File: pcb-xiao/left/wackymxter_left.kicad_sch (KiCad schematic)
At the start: 81 parts, among them U1 xiao-ble, U2 74HC595

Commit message: Insane progresgress
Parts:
- U1: footprint mcu:xiao-ble-smd-cutout -> wackymxter:xiao-ble-smd-cutout
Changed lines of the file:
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@@
 			)
 		)
-		(property "Footprint" "mcu:xiao-ble-smd-cutout"
+		(property "Footprint" "wackymxter:xiao-ble-smd-cutout"
 			(at 39.37 43.18 0)
 			(effects

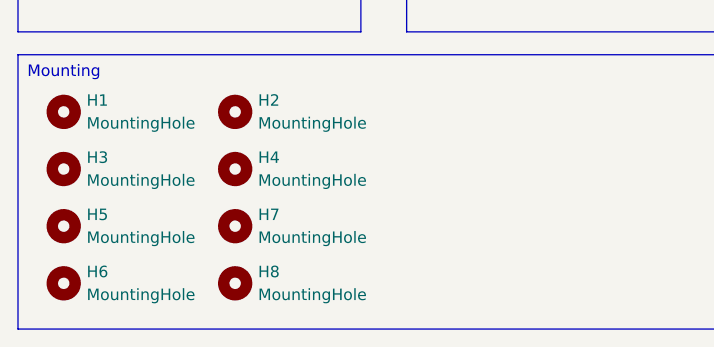
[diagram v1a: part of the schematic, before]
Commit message: Cooler cutout out and match schematics
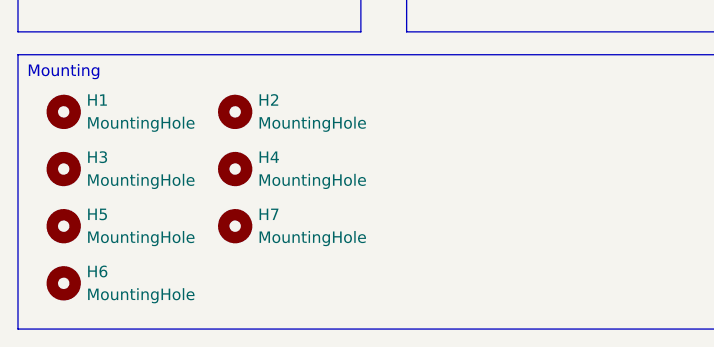
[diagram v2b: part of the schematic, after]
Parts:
- removed H8: MountingHole, MountingHole:MountingHole_2.2mm_M2, symbol Mechanical:MountingHole
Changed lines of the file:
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@@
-	)
-	(symbol
-		(lib_id "Mechanical:MountingHole")
-		(at 40.64 171.45 0)
-		(unit 1)
-		(exclude_from_sim yes)
-		(in_bom no)
-		(on_board yes)
-		(dnp no)
-		(fields_autoplaced yes)
-		(property "Reference" "H8"
-			(at 43.18 170.1799 0)
-			(effects
-				(font
-					(size 1.27 1.27)
-				)
-				(justify left)
-			)
-		)
-		(property "Value" "MountingHole"
-			(at 43.18 172.7199 0)
-			(effects
-				(font
-					(size 1.27 1.27)
-				)
-				(justify left)
-			)
-		)
-		(property "Footprint" "MountingHole:MountingHole_2.2mm_M2"
-			(at 40.64 171.45 0)
-			(effects
-				(font
-					(size 1.27 1.27)
-				)
-				(hide yes)
-			)
-		)
-		(property "Datasheet" "~"
-			(at 40.64 171.45 0)
-			(effects
-				(font
-					(size 1.27 1.27)
-				)
-				(hide yes)
-			)
-		)
-		(property "Description" "Mounting Hole without connection"
-			(at 40.64 171.45 0)
-			(effects
-				(font
-					(size 1.27 1.27)
-				)
-				(hide yes)
-			)
-		)
-		(instances
-			(project "wackymxter"
-				(path "/2f458fa5-a956-4b78-96f1-0e4e52f40df3"
-					(reference "H8")
-					(unit 1)
-				)
-			)
-		)
 	)
 	(symbol
